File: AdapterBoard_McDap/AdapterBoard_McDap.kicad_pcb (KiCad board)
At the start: 2 copper layers, 71.1 x 55.2 mm, 5 parts, among them J1 CN7, J2 CN10, J2_J4 LaunchPad, J3_J1 LaunchPad, J5 RSLK2

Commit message: Fixing some visual stuff
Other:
- board text removed: "Keep this spacing the same for STM Header Pins"
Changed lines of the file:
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@@
 			)
-		)
-		(dimension
-			(type aligned)
-			(layer "F.Fab")
-			(pts
-				(xy 58.5828 93.68) (xy 130.9728 93.68)
-			)
-			(height -15.565)
-			(gr_text "72.3900 mm"
-				(at 94.7778 77.015 0)
-				(layer "F.Fab")
-				(effects
-					(font
-						(size 1 1)
-						(thickness 0.1)
-					)
-				)
-			)
-			(format
-				(prefix "")
-				(suffix "")
-				(units 3)
-				(units_format 1)
-				(precision 4)
-			)
-			(style
-				(thickness 0.1)
-				(arrow_length 1.27)
-				(text_position_mode 0)
-				(extension_height 0.58642)
-				(extension_offset 0.5) keep_text_aligned)
 		)
 	)
@@
 		(layer "Edge.Cuts")
 	)
-	(gr_text "Keep this spacing the same for STM Header Pins\n"
-		(at 205.74 73.66 0)
-		(layer "Dwgs.User")
-		(effects
-			(font
-				(size 1 1)
-				(thickness 0.15)
-			)
-			(justify left bottom)
-		)
-	)
 	(dimension
 		(type aligned)
 		(layer "Dwgs.User")
 		(pts
-			(xy 190.5 81.28) (xy 254 81.28)
+			(xy 64.75 84.33) (xy 128.25 84.33)
 		)
 		(height -10.16)
 		(gr_text "63.5000 mm"
-			(at 222.25 69.97 0)
+			(at 96.5 73.02 0)
 			(layer "Dwgs.User")
 			(effects

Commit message: Added silkscreen image
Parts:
- added G***: LOGO, RSLK2:Rotunda, F.Cu at (98.3, 98.8)
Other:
- board text added: "McDap Bots TI -> STM Adapter Board"

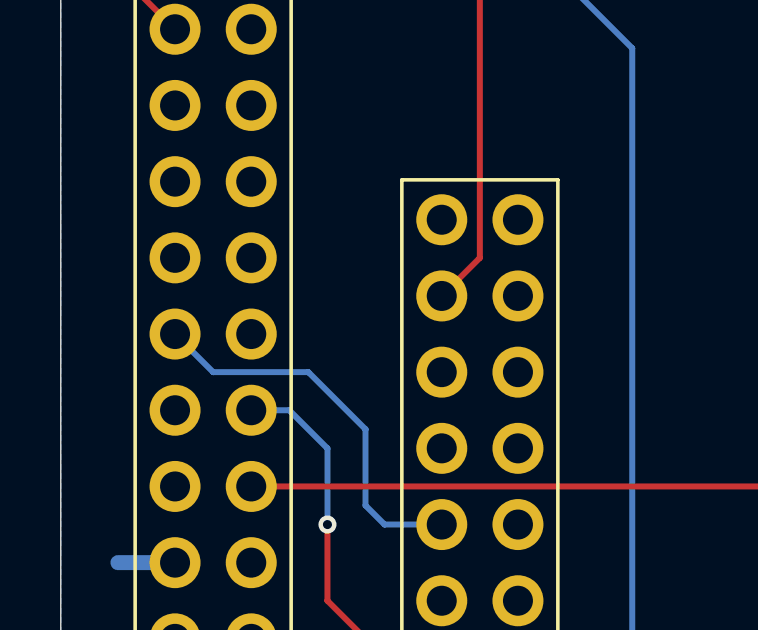
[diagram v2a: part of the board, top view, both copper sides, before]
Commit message: Add missing pin connection between TI and STM
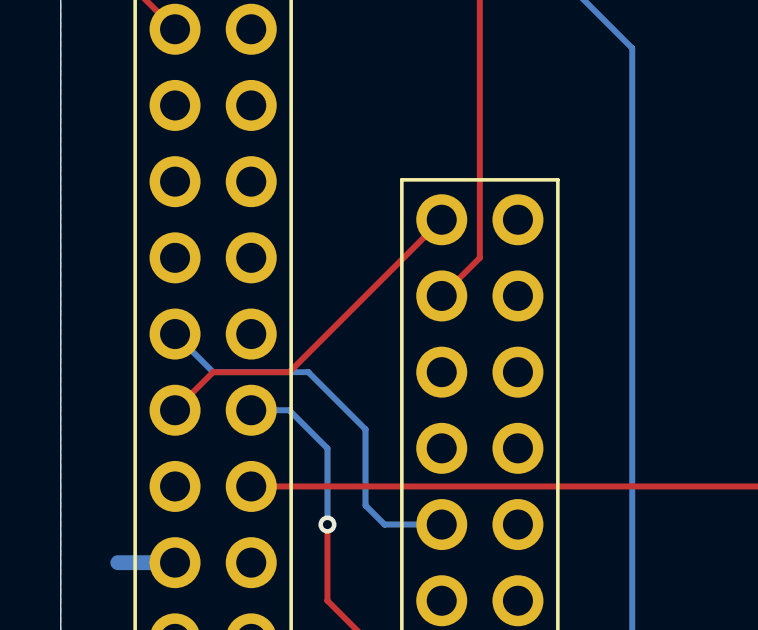
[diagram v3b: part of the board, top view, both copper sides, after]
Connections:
- J2 pad 24: PB_6 -> PB16
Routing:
- net PB16: track 0.00 -> 11.5 mm

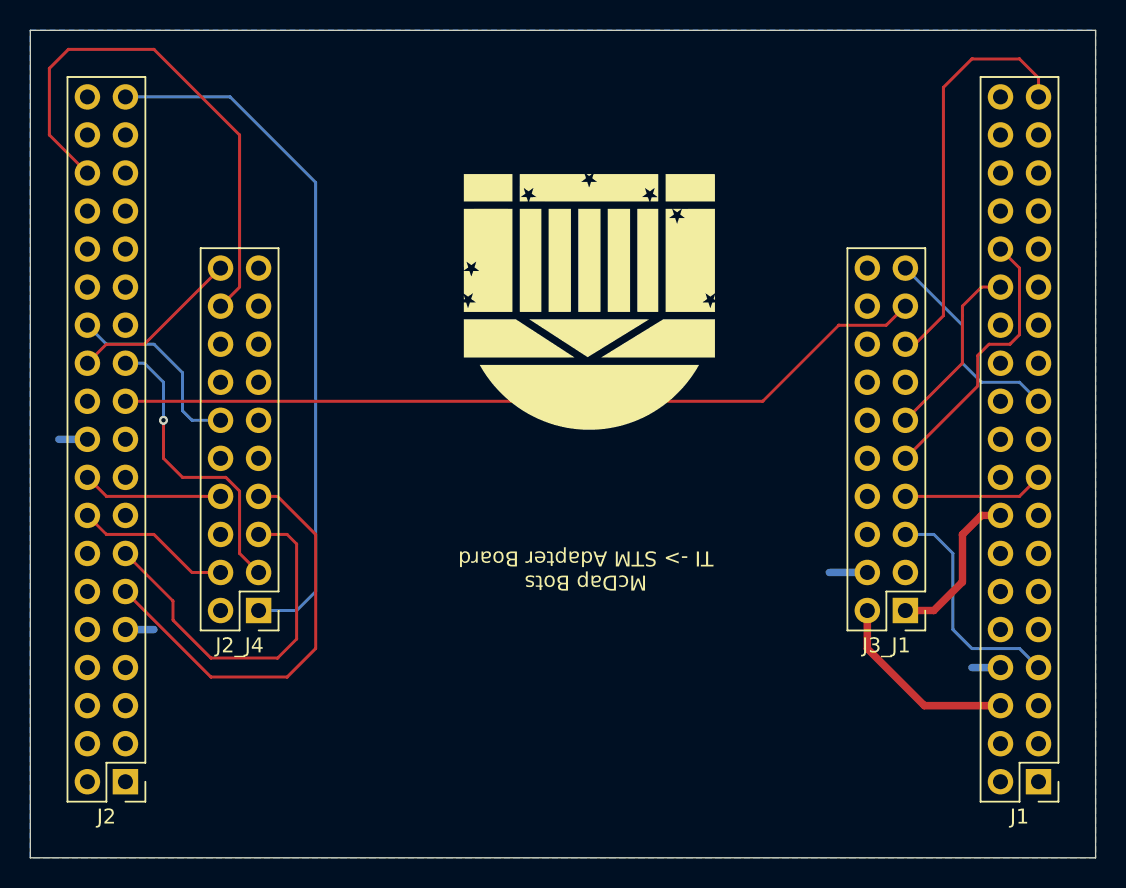
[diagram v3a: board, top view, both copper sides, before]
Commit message: Minor silkscreen improvements
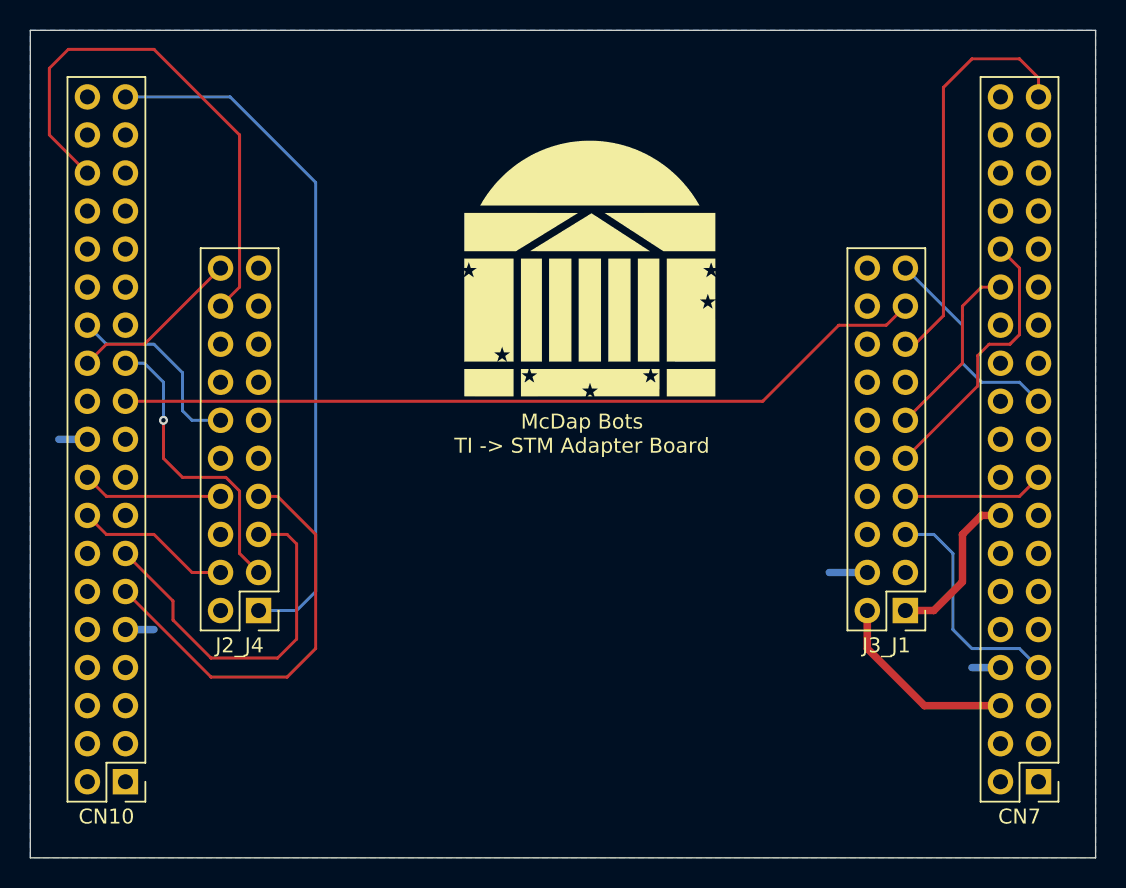
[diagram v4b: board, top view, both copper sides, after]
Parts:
- moved G*** 2.29 mm to (98.3, 96.5), turned to 0 degrees
- renumbered J2 to CN10, J1 to CN7
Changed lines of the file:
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@@
 	(footprint "RSLK2:Rotunda"
 		(layer "F.Cu")
-		(at 98.298 98.806 180)
+		(at 98.298 96.52)
 		(property "Reference" "G***"
-			(at 0 0 0)
+			(at 0 0 360)
 			(layer "F.SilkS")
 			(hide yes)
@@
 		)
 		(property "Value" "LOGO"
-			(at 0.75 0 0)
+			(at 0.75 0 360)
 			(layer "F.SilkS")
 			(hide yes)
@@
 		)
 		(property "Footprint" ""
-			(at 0 0 0)
+			(at 0 0 360)
 			(layer "F.Fab")
 			(hide yes)
@@
 		)
 		(property "Datasheet" ""
-			(at 0 0 0)
+			(at 0 0 360)
 			(layer "F.Fab")
 			(hide yes)
@@
 		)
 		(property "Description" ""
-			(at 0 0 0)
+			(at 0 0 360)
 			(layer "F.Fab")
 			(hide yes)
@@
 		(fp_poly
 			(pts
-				(xy 8.396064 7.6505) (xy 8.396064 8.56551) (xy 6.773616 8.56551) (xy 5.151168 8.56551) (xy 5.151168 7.6505)
-				(xy 5.151168 6.73549) (xy 6.773616 6.73549) (xy 8.396064 6.73549)
+				(xy -3.18559 2.804336) (xy -3.18559 6.244096) (xy -3.884556 6.244096) (xy -4.583522 6.244096) (xy -4.583522 2.804336)
+				(xy -4.583522 -0.635424) (xy -3.884556 -0.635424) (xy -3.18559 -0.635424)
 			)
 			(stroke
@@
 		(fp_poly
 			(pts
-				(xy 4.659774 2.804336) (xy 4.659774 6.244096) (xy 3.939627 6.244096) (xy 3.21948 6.244096) (xy 3.21948 2.804336)
-				(xy 3.21948 -0.635424) (xy 3.939627 -0.635424) (xy 4.659774 -0.635424)
+				(xy -1.211541 2.804336) (xy -1.211541 6.244096) (xy -1.957104 6.244096) (xy -2.702668 6.244096)
+				(xy -2.702668 2.804336) (xy -2.702668 -0.635424) (xy -1.957104 -0.635424) (xy -1.211541 -0.635424)
 			)
 			(stroke
@@
 		(fp_poly
 			(pts
-				(xy 2.736558 2.804336) (xy 2.736558 6.244096) (xy 1.990994 6.244096) (xy 1.245431 6.244096) (xy 1.245431 2.804336)
-				(xy 1.245431 -0.635424) (xy 1.990994 -0.635424) (xy 2.736558 -0.635424)
+				(xy 0.762509 2.804336) (xy 0.762509 6.244096) (xy 0.016945 6.244096) (xy -0.728619 6.244096) (xy -0.728619 2.804336)
+				(xy -0.728619 -0.635424) (xy 0.016945 -0.635424) (xy 0.762509 -0.635424)
 			)
 			(stroke
@@
 		(fp_poly
 			(pts
-				(xy 0.762509 2.804336) (xy 0.762509 6.244096) (xy 0.016945 6.244096) (xy -0.728619 6.244096) (xy -0.728619 2.804336)
-				(xy -0.728619 -0.635424) (xy 0.016945 -0.635424) (xy 0.762509 -0.635424)
+				(xy 2.736558 2.804336) (xy 2.736558 6.244096) (xy 1.990994 6.244096) (xy 1.245431 6.244096) (xy 1.245431 2.804336)
+				(xy 1.245431 -0.635424) (xy 1.990994 -0.635424) (xy 2.736558 -0.635424)
 			)
 			(stroke
@@
 		(fp_poly
 			(pts
-				(xy -1.211541 2.804336) (xy -1.211541 6.244096) (xy -1.957104 6.244096) (xy -2.702668 6.244096)
-				(xy -2.702668 2.804336) (xy -2.702668 -0.635424) (xy -1.957104 -0.635424) (xy -1.211541 -0.635424)
+				(xy 4.659774 2.804336) (xy 4.659774 6.244096) (xy 3.939627 6.244096) (xy 3.21948 6.244096) (xy 3.21948 2.804336)
+				(xy 3.21948 -0.635424) (xy 3.939627 -0.635424) (xy 4.659774 -0.635424)
 			)
 			(stroke
@@
 		(fp_poly
 			(pts
-				(xy -3.18559 2.804336) (xy -3.18559 6.244096) (xy -3.884556 6.244096) (xy -4.583522 6.244096) (xy -4.583522 2.804336)
-				(xy -4.583522 -0.635424) (xy -3.884556 -0.635424) (xy -3.18559 -0.635424)
+				(xy 8.396064 7.6505) (xy 8.396064 8.56551) (xy 6.773616 8.56551) (xy 5.151168 8.56551) (xy 5.151168 7.6505)
+				(xy 5.151168 6.73549) (xy 6.773616 6.73549) (xy 8.396064 6.73549)
 			)
 			(stroke
@@
 		(fp_poly
 			(pts
-				(xy 8.396064 -2.406137) (xy 8.396064 -1.126818) (xy 6.661358 -1.127593) (xy 4.926651 -1.128368)
-				(xy 2.968029 -2.400558) (xy 2.80209 -2.50835) (xy 2.63984 -2.613761) (xy 2.481857 -2.716416) (xy 2.328715 -2.81594)
-				(xy 2.18099 -2.911961) (xy 2.039258 -3.004102) (xy 1.904093 -3.09199) (xy 1.776071 -3.175251) (xy 1.655769 -3.253509)
-				(xy 1.54376 -3.32639) (xy 1.440622 -3.39352) (xy 1.346928 -3.454524) (xy 1.263255 -3.509028) (xy 1.190179 -3.556658)
-				(xy 1.128273 -3.597038) (xy 1.078115 -3.629795) (xy 1.040279 -3.654554) (xy 1.015342 -3.670941)
-				(xy 1.003877 -3.67858) (xy 1.003158 -3.679103) (xy 1.011116 -3.679531) (xy 1.035476 -3.679952) (xy 1.075698 -3.680365)
-				(xy 1.13124 -3.680768) (xy 1.20156 -3.681161) (xy 1.286117 -3.681543) (xy 1.384369 -3.681913) (xy 1.495774 -3.68227)
-				(xy 1.619792 -3.682613) (xy 1.75588 -3.682942) (xy 1.903496 -3.683254) (xy 2.0621 -3.68355) (xy 2.231149 -3.683828)
-				(xy 2.410103 -3.684087) (xy 2.598418 -3.684327) (xy 2.795555 -3.684547) (xy 3.000971 -3.684745)
-				(xy 3.214124 -3.684921) (xy 3.434474 -3.685074) (xy 3.661478 -3.685202) (xy 3.894595 -3.685306)
-				(xy 4.133284 -3.685383) (xy 4.377002 -3.685433) (xy 4.625208 -3.685456) (xy 4.696487 -3.685457)
-				(xy 8.396064 -3.685457)
-			)
-			(stroke
-				(width 0)
-				(type solid)
-			)
-			(fill solid)
-			(layer "F.SilkS")
-		)
-		(fp_poly
-			(pts
 				(xy -4.303387 -3.685441) (xy -4.043496 -3.685392) (xy -3.789928 -3.685313) (xy -3.543162 -3.685204)
 				(xy -3.303678 -3.685066) (xy -3.071956 -3.684899) (xy -2.848477 -3.684705) (xy -2.633721 -3.684485)
@@
 		(fp_poly
 			(pts
+				(xy 8.396064 -2.406137) (xy 8.396064 -1.126818) (xy 6.661358 -1.127593) (xy 4.926651 -1.128368)
+				(xy 2.968029 -2.400558) (xy 2.80209 -2.50835) (xy 2.63984 -2.613761) (xy 2.481857 -2.716416) (xy 2.328715 -2.81594)
+				(xy 2.18099 -2.911961) (xy 2.039258 -3.004102) (xy 1.904093 -3.09199) (xy 1.776071 -3.175251) (xy 1.655769 -3.253509)
+				(xy 1.54376 -3.32639) (xy 1.440622 -3.39352) (xy 1.346928 -3.454524) (xy 1.263255 -3.509028) (xy 1.190179 -3.556658)
+				(xy 1.128273 -3.597038) (xy 1.078115 -3.629795) (xy 1.040279 -3.654554) (xy 1.015342 -3.670941)
+				(xy 1.003877 -3.67858) (xy 1.003158 -3.679103) (xy 1.011116 -3.679531) (xy 1.035476 -3.679952) (xy 1.075698 -3.680365)
+				(xy 1.13124 -3.680768) (xy 1.20156 -3.681161) (xy 1.286117 -3.681543) (xy 1.384369 -3.681913) (xy 1.495774 -3.68227)
+				(xy 1.619792 -3.682613) (xy 1.75588 -3.682942) (xy 1.903496 -3.683254) (xy 2.0621 -3.68355) (xy 2.231149 -3.683828)
+				(xy 2.410103 -3.684087) (xy 2.598418 -3.684327) (xy 2.795555 -3.684547) (xy 3.000971 -3.684745)
+				(xy 3.214124 -3.684921) (xy 3.434474 -3.685074) (xy 3.661478 -3.685202) (xy 3.894595 -3.685306)
+				(xy 4.133284 -3.685383) (xy 4.377002 -3.685433) (xy 4.625208 -3.685456) (xy 4.696487 -3.685457)
+				(xy 8.396064 -3.685457)
+			)
+			(stroke
+				(width 0)
+				(type solid)
+			)
+			(fill solid)
+			(layer "F.SilkS")
+		)
+		(fp_poly
+			(pts
 				(xy 0.094311 -8.505727) (xy 0.191677 -8.504954) (xy 0.283303 -8.503571) (xy 0.365951 -8.501579)
 				(xy 0.436381 -8.498977) (xy 0.46292 -8.497625) (xy 0.841154 -8.46816) (xy 1.213342 -8.422946) (xy 1.579933 -8.361885)
@@
 		(descr "Through hole straight pin header, 2x19, 2.54mm pitch, double rows")
 		(tags "Through hole pin header THT 2x19 2.54mm double row")
-		(property "Reference" "J2"
+		(property "Reference" "CN10"
 			(at 1.27 -2.33 0)
 			(layer "F.SilkS")
@@
 		(descr "Through hole straight pin header, 2x19, 2.54mm pitch, double rows")
 		(tags "Through hole pin header THT 2x19 2.54mm double row")
-		(property "Reference" "J1"
+		(property "Reference" "CN7"
 			(at 1.27 -2.33 0)
 			(layer "F.SilkS")
@@
 	)
 	(gr_text "McDap Bots \nTI -> STM Adapter Board"
-		(at 98.044 115.316 180)
+		(at 97.79 108.966 0)
 		(layer "F.SilkS")
 		(effects
